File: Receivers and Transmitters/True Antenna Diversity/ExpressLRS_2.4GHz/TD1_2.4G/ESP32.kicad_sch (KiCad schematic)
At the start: 10 parts, among them U8 ESP32-PICO-D4

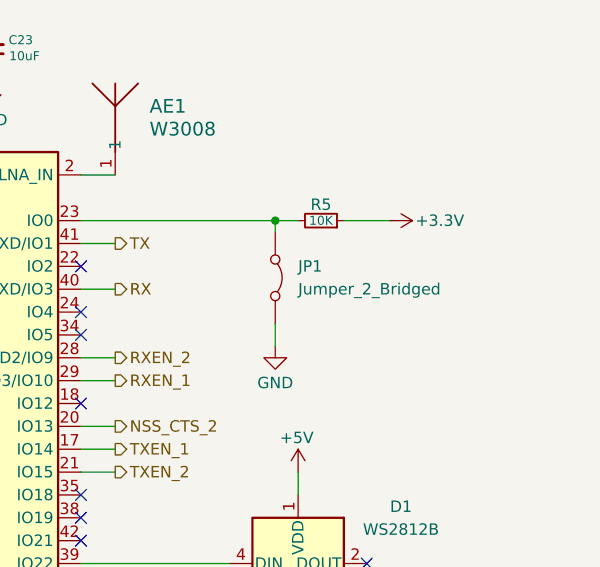
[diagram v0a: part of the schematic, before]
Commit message: Update True Antenna Diversity TD1_2.4G KiCad schematics and PCB design
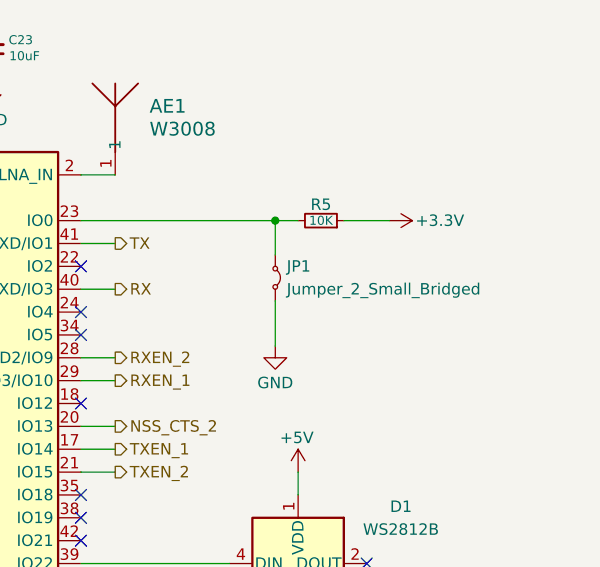
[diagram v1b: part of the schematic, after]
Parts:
- removed JP1: Jumper_2_Bridged, TestPoint:TestPoint_2Pads_Pitch2.54mm_Drill0.8mm, symbol Jumper:Jumper_2_Bridged
- added JP1: Jumper_2_Small_Bridged, TestPoint:TestPoint_2Pads_Pitch2.54mm_Drill0.8mm, symbol Jumper:Jumper_2_Small_Bridged
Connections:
- net GND: now also JP1.2 (B)
- net at R5.2, U8.23 (IO0): now also JP1.1 (A)
